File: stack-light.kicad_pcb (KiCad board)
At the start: 2 copper layers, 82 x 56.5 mm, 125 parts, among them J2 Mini-DIN-6, J3 Barrel_Jack_Switch, J4 USB_C_Receptacle_USB2.0, Q1 2N7002, Q2 2N7002, Q3 2N7002, Q4 2N7002, Q5 2N7002, Q6 BC817-40, Q7 BC817-40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

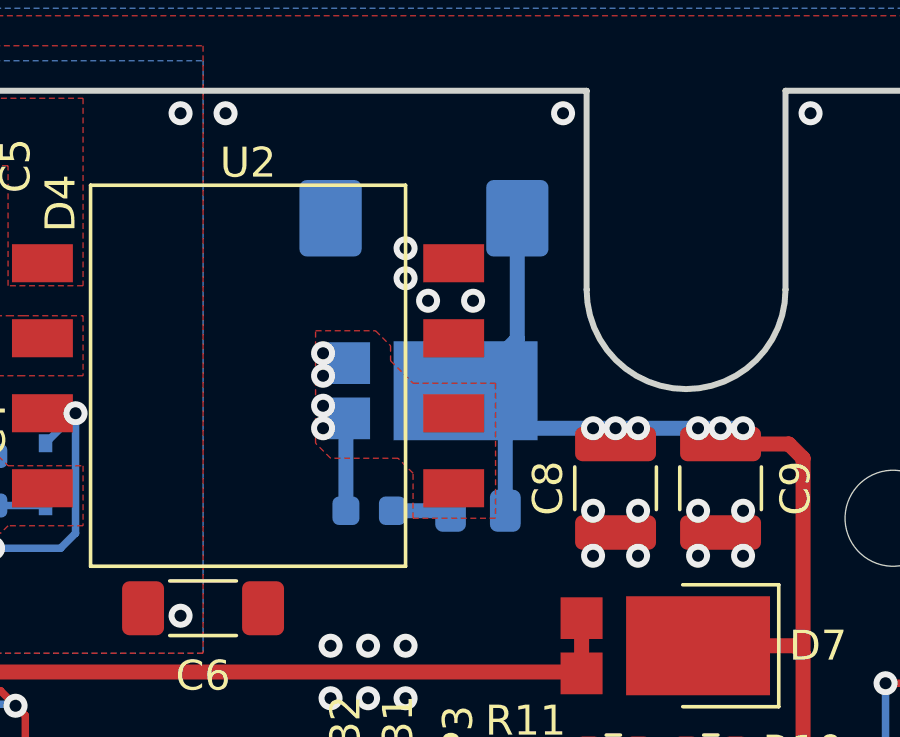
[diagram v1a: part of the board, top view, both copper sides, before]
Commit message: Corrected Footprint for POE transformers, PCB updated for correct footprint
The POE transformer had the order of its pinout on the higher numbered side reversed so the pairs of output pins were connected back to front. This change fixes this
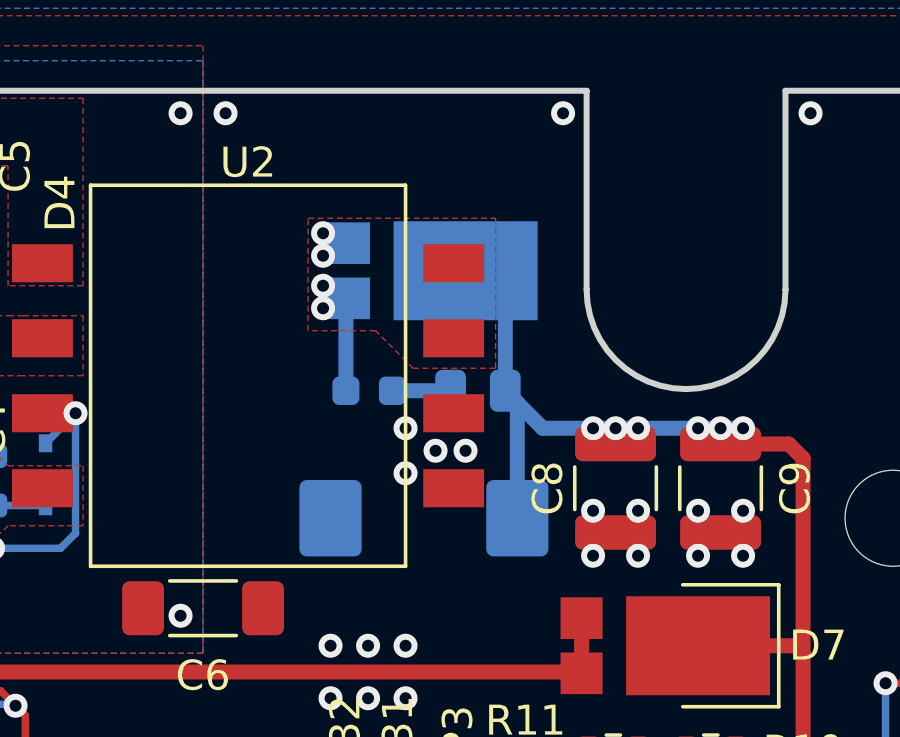
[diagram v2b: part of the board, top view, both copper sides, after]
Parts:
- moved C10 10.0 mm to (152.4, 64.2)
- moved C7 4.00 mm to (150.5, 60.0)
- moved D6 4.00 mm to (152.6, 56.0)
- moved R8 4.00 mm to (154.2, 60.0)
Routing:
- net +12V: track 49.7 -> 48.1 mm

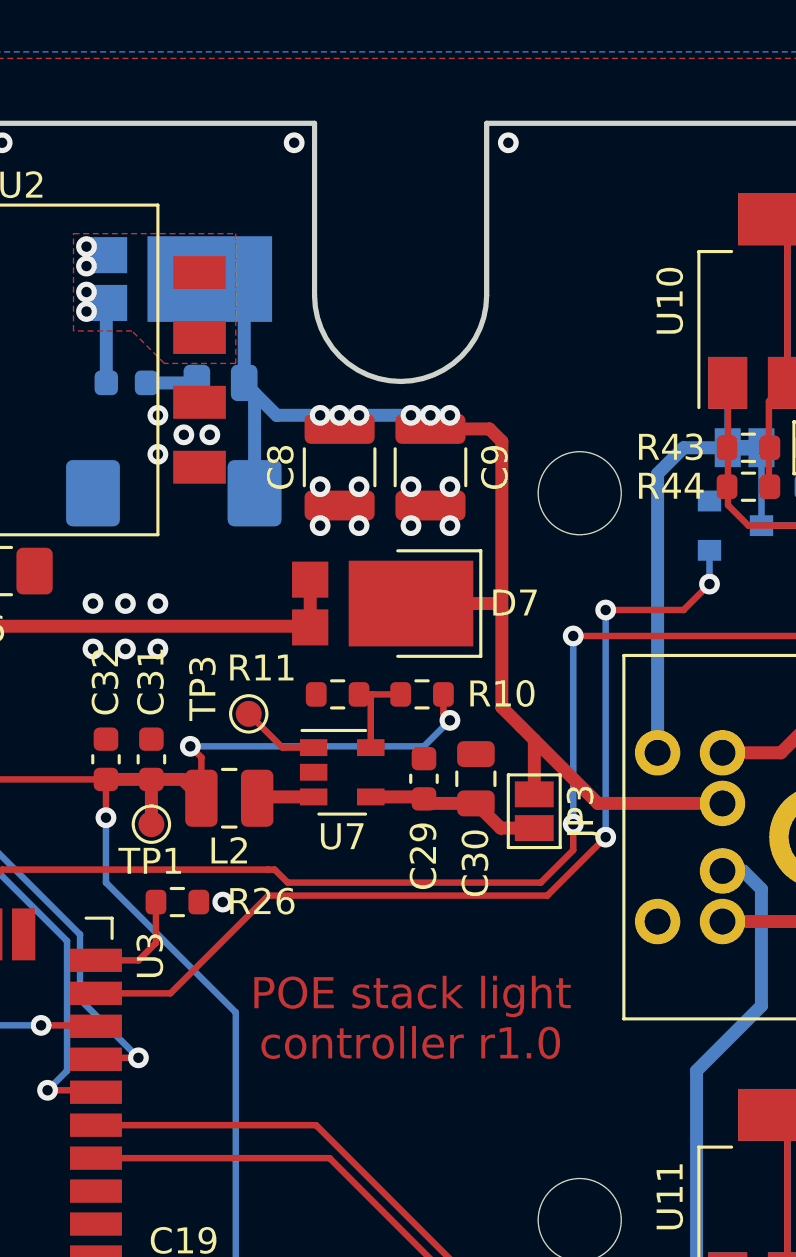
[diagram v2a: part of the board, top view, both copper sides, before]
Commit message: Add schematic edits to PCB
Add load resistors for POE power supply
Add pulldown for buzzer output channel
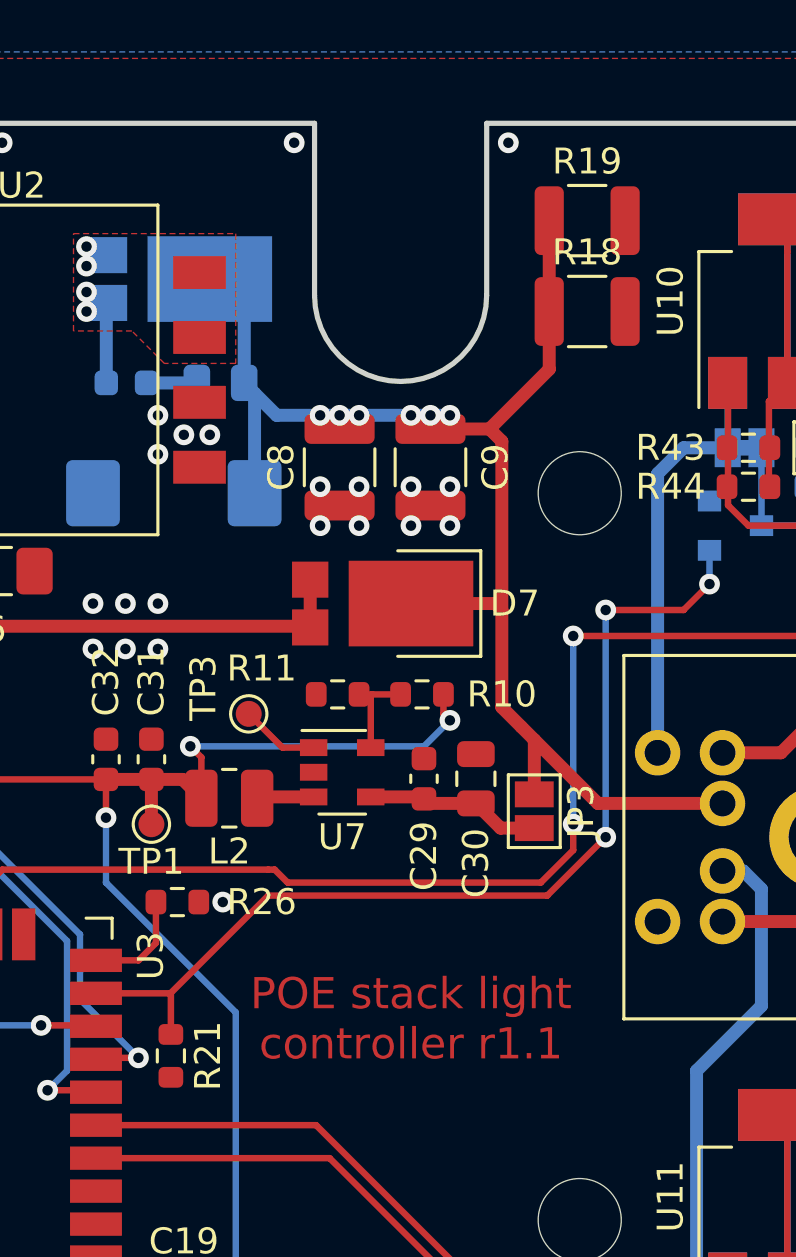
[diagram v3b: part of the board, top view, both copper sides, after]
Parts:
- added R18: 330, Resistor_SMD:R_1210_3225Metric, F.Cu at (168.3, 57.2)
- added R19: DNP, Resistor_SMD:R_1210_3225Metric, F.Cu at (168.3, 53.8)
- added R21: 10k, Resistor_SMD:R_0603_1608Metric, F.Cu at (152.2, 85.9)
- R28: value 10k -> DNP
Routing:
- net +12V: track 48.1 -> 57.1 mm
- net Buzzer: track 36.6 -> 38.2 mm
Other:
- board text added: "POE stack light controller r1.1"
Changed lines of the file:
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@@
     (thickness 1.6)
     (drawings 22)
-    (tracks 921)
+    (tracks 926)
     (zones 0)
-    (modules 125)
+    (modules 128)
     (nets 131)
   )
@@
     (add_net Yellow)
   )
+  (module Resistor_SMD:R_0603_1608Metric (layer F.Cu)
+    (at 152.25 85.925 270)
+    (descr "Resistor SMD 0603 (1608 Metric), square (rectangular) end terminal, IPC_7351 nominal, (Body size source: IPC-SM-782 page 72, https://www.pcb-3d.com/wordpress/wp-content/uploads/ipc-sm-782a_amendment_1_and_2.pdf), generated with kicad-footprint-generator")
+    (tags resistor)
+    (attr smd)
+    (fp_text reference R21 (at 0 -1.43 90) (layer F.SilkS)
+      (effects (font (size 1 1) (thickness 0.15)))
+    )
+    (fp_text value 10k (at 0 1.43 90) (layer F.Fab)
+      (effects (font (size 1 1) (thickness 0.15)))
+    )
+    (fp_line (start 1.48 0.73) (end -1.48 0.73) (layer F.CrtYd) (width 0.05))
+    (fp_line (start 1.48 -0.73) (end 1.48 0.73) (layer F.CrtYd) (width 0.05))
+    (fp_line (start -1.48 -0.73) (end 1.48 -0.73) (layer F.CrtYd) (width 0.05))
+    (fp_line (start -1.48 0.73) (end -1.48 -0.73) (layer F.CrtYd) (width 0.05))
+    (fp_line (start -0.237258 0.5225) (end 0.237258 0.5225) (layer F.SilkS) (width 0.12))
+    (fp_line (start -0.237258 -0.5225) (end 0.237258 -0.5225) (layer F.SilkS) (width 0.12))
+    (fp_line (start 0.8 0.4125) (end -0.8 0.4125) (layer F.Fab) (width 0.1))
+    (fp_line (start 0.8 -0.4125) (end 0.8 0.4125) (layer F.Fab) (width 0.1))
+    (fp_line (start -0.8 -0.4125) (end 0.8 -0.4125) (layer F.Fab) (width 0.1))
+    (fp_line (start -0.8 0.4125) (end -0.8 -0.4125) (layer F.Fab) (width 0.1))
+    (fp_text user %R (at 0 0 90) (layer F.Fab)
+      (effects (font (size 0.4 0.4) (thickness 0.06)))
+    )
+    (pad 2 smd roundrect (at 0.825 0 270) (size 0.8 0.95) (layers F.Cu F.Paste F.Mask) (roundrect_rratio 0.25)
+      (net 6 GND))
+    (pad 1 smd roundrect (at -0.825 0 270) (size 0.8 0.95) (layers F.Cu F.Paste F.Mask) (roundrect_rratio 0.25)
+      (net 27 Buzzer))
+    (model ${KISYS3DMOD}/Resistor_SMD.3dshapes/R_0603_1608Metric.wrl
+      (at (xyz 0 0 0))
+      (scale (xyz 1 1 1))
+      (rotate (xyz 0 0 0))
+    )
+  )
+  (module Resistor_SMD:R_1210_3225Metric (layer F.Cu)
+    (at 168.2875 53.75)
+    (descr "Resistor SMD 1210 (3225 Metric), square (rectangular) end terminal, IPC_7351 nominal, (Body size source: IPC-SM-782 page 72, https://www.pcb-3d.com/wordpress/wp-content/uploads/ipc-sm-782a_amendment_1_and_2.pdf), generated with kicad-footprint-generator")
+    (tags resistor)
+    (attr smd)
+    (fp_text reference R19 (at 0 -2.28) (layer F.SilkS)
+      (effects (font (size 1 1) (thickness 0.15)))
+    )
+    (fp_text value DNP (at 0 2.28) (layer F.Fab)
+      (effects (font (size 1 1) (thickness 0.15)))
+    )
+    (fp_line (start 2.28 1.58) (end -2.28 1.58) (layer F.CrtYd) (width 0.05))
+    (fp_line (start 2.28 -1.58) (end 2.28 1.58) (layer F.CrtYd) (width 0.05))
+    (fp_line (start -2.28 -1.58) (end 2.28 -1.58) (layer F.CrtYd) (width 0.05))
+    (fp_line (start -2.28 1.58) (end -2.28 -1.58) (layer F.CrtYd) (width 0.05))
+    (fp_line (start -0.723737 1.355) (end 0.723737 1.355) (layer F.SilkS) (width 0.12))
+    (fp_line (start -0.723737 -1.355) (end 0.723737 -1.355) (layer F.SilkS) (width 0.12))
+    (fp_line (start 1.6 1.245) (end -1.6 1.245) (layer F.Fab) (width 0.1))
+    (fp_line (start 1.6 -1.245) (end 1.6 1.245) (layer F.Fab) (width 0.1))
+    (fp_line (start -1.6 -1.245) (end 1.6 -1.245) (layer F.Fab) (width 0.1))
+    (fp_line (start -1.6 1.245) (end -1.6 -1.245) (layer F.Fab) (width 0.1))
+    (fp_text user %R (at 0 0) (layer F.Fab)
+      (effects (font (size 0.8 0.8) (thickness 0.12)))
+    )
+    (pad 2 smd roundrect (at 1.4625 0) (size 1.125 2.65) (layers F.Cu F.Paste F.Mask) (roundrect_rratio 0.222222)
+      (net 6 GND))
+    (pad 1 smd roundrect (at -1.4625 0) (size 1.125 2.65) (layers F.Cu F.Paste F.Mask) (roundrect_rratio 0.222222)
+      (net 9 +12V))
+    (model ${KISYS3DMOD}/Resistor_SMD.3dshapes/R_1210_3225Metric.wrl
+      (at (xyz 0 0 0))
+      (scale (xyz 1 1 1))
+      (rotate (xyz 0 0 0))
+    )
+  )
+  (module Resistor_SMD:R_1210_3225Metric (layer F.Cu)
+    (at 168.2875 57.25)
+    (descr "Resistor SMD 1210 (3225 Metric), square (rectangular) end terminal, IPC_7351 nominal, (Body size source: IPC-SM-782 page 72, https://www.pcb-3d.com/wordpress/wp-content/uploads/ipc-sm-782a_amendment_1_and_2.pdf), generated with kicad-footprint-generator")
+    (tags resistor)
+    (attr smd)
+    (fp_text reference R18 (at 0 -2.28) (layer F.SilkS)
+      (effects (font (size 1 1) (thickness 0.15)))
+    )
+    (fp_text value 330 (at 0 2.28) (layer F.Fab)
+      (effects (font (size 1 1) (thickness 0.15)))
+    )
+    (fp_line (start 2.28 1.58) (end -2.28 1.58) (layer F.CrtYd) (width 0.05))
+    (fp_line (start 2.28 -1.58) (end 2.28 1.58) (layer F.CrtYd) (width 0.05))
+    (fp_line (start -2.28 -1.58) (end 2.28 -1.58) (layer F.CrtYd) (width 0.05))
+    (fp_line (start -2.28 1.58) (end -2.28 -1.58) (layer F.CrtYd) (width 0.05))
+    (fp_line (start -0.723737 1.355) (end 0.723737 1.355) (layer F.SilkS) (width 0.12))
+    (fp_line (start -0.723737 -1.355) (end 0.723737 -1.355) (layer F.SilkS) (width 0.12))
+    (fp_line (start 1.6 1.245) (end -1.6 1.245) (layer F.Fab) (width 0.1))
+    (fp_line (start 1.6 -1.245) (end 1.6 1.245) (layer F.Fab) (width 0.1))
+    (fp_line (start -1.6 -1.245) (end 1.6 -1.245) (layer F.Fab) (width 0.1))
+    (fp_line (start -1.6 1.245) (end -1.6 -1.245) (layer F.Fab) (width 0.1))
+    (fp_text user %R (at 0 0) (layer F.Fab)
+      (effects (font (size 0.8 0.8) (thickness 0.12)))
+    )
+    (pad 2 smd roundrect (at 1.4625 0) (size 1.125 2.65) (layers F.Cu F.Paste F.Mask) (roundrect_rratio 0.222222)
+      (net 6 GND))
+    (pad 1 smd roundrect (at -1.4625 0) (size 1.125 2.65) (layers F.Cu F.Paste F.Mask) (roundrect_rratio 0.222222)
+      (net 9 +12V))
+    (model ${KISYS3DMOD}/Resistor_SMD.3dshapes/R_1210_3225Metric.wrl
+      (at (xyz 0 0 0))
+      (scale (xyz 1 1 1))
+      (rotate (xyz 0 0 0))
+    )
+  )
   (module stack-light:Transformer_Coilcraft_POE70P (layer F.Cu)
     (at 146.5 59.5)
@@
       (effects (font (size 1 1) (thickness 0.15)) (justify mirror))
     )
-    (fp_text value 10k (at 0 -1.43) (layer B.Fab)
+    (fp_text value DNP (at 0 -1.43) (layer B.Fab)
       (effects (font (size 1 1) (thickness 0.15)) (justify mirror))
     )
@@
     (effects (font (size 1.2 1.2) (thickness 0.3)))
   )
-  (gr_text "POE stack light\ncontroller r1.0" (at 161.5 84.5) (layer F.Cu)
+  (gr_text "POE stack light\ncontroller r1.1" (at 161.5 84.5) (layer F.Cu)
     (effects (font (size 1.2 1.2) (thickness 0.3)))
   )
@@
   (segment (start 155.475 60.4) (end 155.075 60) (width 0.5) (layer B.Cu) (net 9))
   (segment (start 155.475 64.25) (end 155.475 60.4) (width 0.5) (layer B.Cu) (net 9))
+  (segment (start 166.825 53.75) (end 166.825 57.25) (width 0.5) (layer F.Cu) (net 9))
+  (segment (start 166.825 59.475) (end 164.525 61.775) (width 0.5) (layer F.Cu) (net 9))
+  (segment (start 166.825 57.25) (end 166.825 59.475) (width 0.5) (layer F.Cu) (net 9))
   (segment (start 136.95 70.45) (end 137.75 70.45) (width 0.25) (layer B.Cu) (net 10))
   (segment (start 140.05 78.5) (end 140.05 77.7) (width 0.25) (layer B.Cu) (net 10))
@@
   (segment (start 172 68.75) (end 173 67.75) (width 0.25) (layer F.Cu) (net 27))
   (segment (start 173 67.75) (end 173 66.45) (width 0.25) (layer B.Cu) (net 27))
+  (segment (start 152.25 83.53) (end 152.235 83.515) (width 0.25) (layer F.Cu) (net 27))
+  (segment (start 152.25 85.1) (end 152.25 83.53) (width 0.25) (layer F.Cu) (net 27))
   (segment (start 176.7125 98.5) (end 176.7125 97) (width 0.25) (layer B.Cu) (net 28))
   (segment (start 176.7125 95.2125) (end 176 94.5) (width 0.25) (layer B.Cu) (net 28))

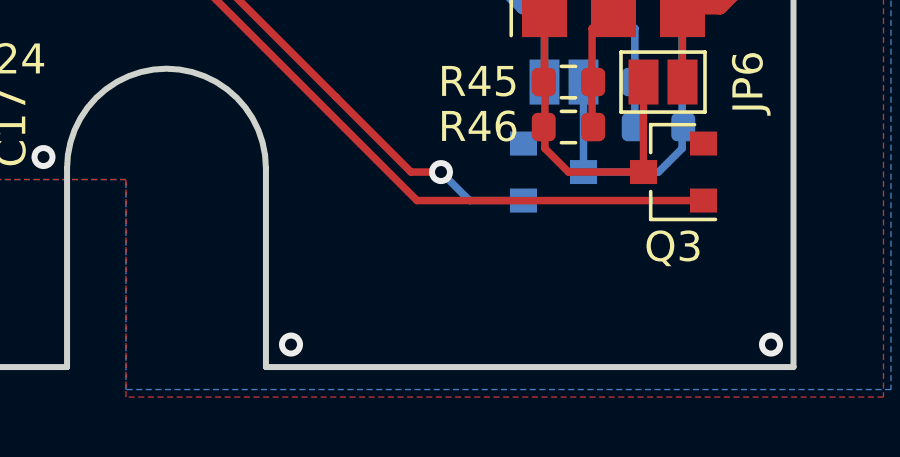
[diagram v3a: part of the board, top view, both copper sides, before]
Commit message: Fix small power supply issues
Update POE class resistor to 62 ohms (class 2)
Increase auxiliary winding limit resistor to 5.1k to comply with device current clamp limit
Add Ground test loop
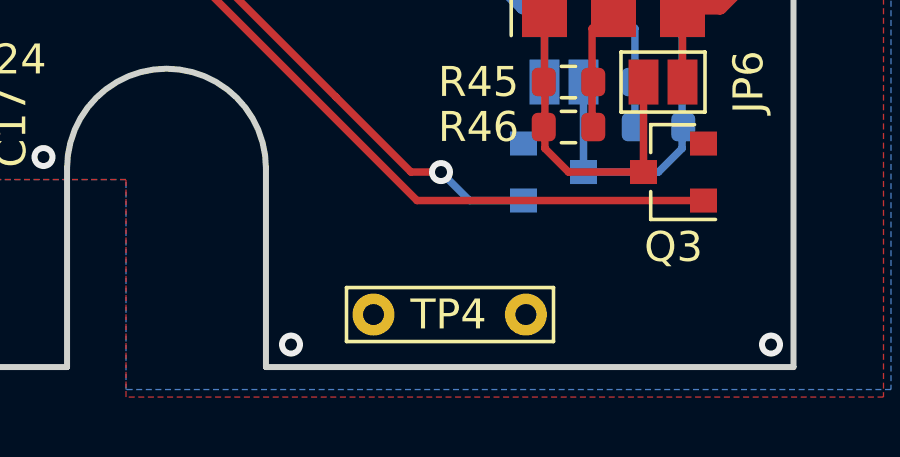
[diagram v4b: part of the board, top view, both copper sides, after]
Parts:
- added TP4: TestPoint, TestPoint:TestPoint_Bridge_Pitch5.08mm_Drill0.7mm, F.Cu at (168.0, 104.8)
- R1: value 41R2 -> 62
- R7: value 1K -> 5K1
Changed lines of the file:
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@@
     (tracks 926)
     (zones 0)
-    (modules 128)
+    (modules 129)
     (nets 131)
   )
@@
     (add_net Yellow)
   )
+  (module TestPoint:TestPoint_Bridge_Pitch5.08mm_Drill0.7mm (layer F.Cu)
+    (at 168 104.75)
+    (descr "wire loop as test point, pitch 5.08mm, hole diameter 0.7mm, wire diameter 1.0mm")
+    (tags "test point wire loop")
+    (fp_text reference TP4 (at 2.5 0) (layer F.SilkS)
+      (effects (font (size 1 1) (thickness 0.15)))
+    )
+    (fp_text value TestPoint (at 1 -1.7) (layer F.Fab)
+      (effects (font (size 1 1) (thickness 0.15)))
+    )
+    (fp_line (start 6.28 1.2) (end -1.2 1.2) (layer F.CrtYd) (width 0.05))
+    (fp_line (start 6.28 1.2) (end 6.28 -1.2) (layer F.CrtYd) (width 0.05))
+    (fp_line (start -1.2 -1.2) (end -1.2 1.2) (layer F.CrtYd) (width 0.05))
+    (fp_line (start -1.2 -1.2) (end 6.28 -1.2) (layer F.CrtYd) (width 0.05))
+    (fp_line (start 5.08 0) (end 0 0) (layer F.Fab) (width 0.12))
+    (fp_line (start -0.9 0.9) (end -0.9 -0.9) (layer F.SilkS) (width 0.12))
+    (fp_line (start 6 0.9) (end -0.9 0.9) (layer F.SilkS) (width 0.12))
+    (fp_line (start 6 -0.9) (end 6 0.9) (layer F.SilkS) (width 0.12))
+    (fp_line (start -0.9 -0.9) (end 6 -0.9) (layer F.SilkS) (width 0.12))
+    (fp_text user %R (at 2.8 1.9) (layer F.Fab)
+      (effects (font (size 1 1) (thickness 0.15)))
+    )
+    (pad 1 thru_hole circle (at 5.08 0) (size 1.4 1.4) (drill 0.7) (layers *.Cu *.Mask)
+      (net 6 GND))
+    (pad 1 thru_hole circle (at 0 0) (size 1.4 1.4) (drill 0.7) (layers *.Cu *.Mask)
+      (net 6 GND))
+    (model ${KISYS3DMOD}/TestPoint.3dshapes/TestPoint_Bridge_Pitch5.08mm_Drill0.7mm.wrl
+      (at (xyz 0 0 0))
+      (scale (xyz 1 1 1))
+      (rotate (xyz 0 0 0))
+    )
+  )
   (module Resistor_SMD:R_0603_1608Metric (layer F.Cu)
     (at 152.25 85.925 270)
@@
       (effects (font (size 1 1) (thickness 0.15)) (justify mirror))
     )
-    (fp_text value 1K (at 0 -1.43 90) (layer B.Fab)
+    (fp_text value 5K1 (at 0 -1.43 90) (layer B.Fab)
       (effects (font (size 1 1) (thickness 0.15)) (justify mirror))
     )
@@
       (effects (font (size 1 1) (thickness 0.15)))
     )
-    (fp_text value 41R2 (at 0 1.43 90) (layer F.Fab)
+    (fp_text value 62 (at 0 1.43 90) (layer F.Fab)
       (effects (font (size 1 1) (thickness 0.15)))
     )
